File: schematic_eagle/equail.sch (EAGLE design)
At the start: 4 parts, among them U1 ATTINY85V-10P

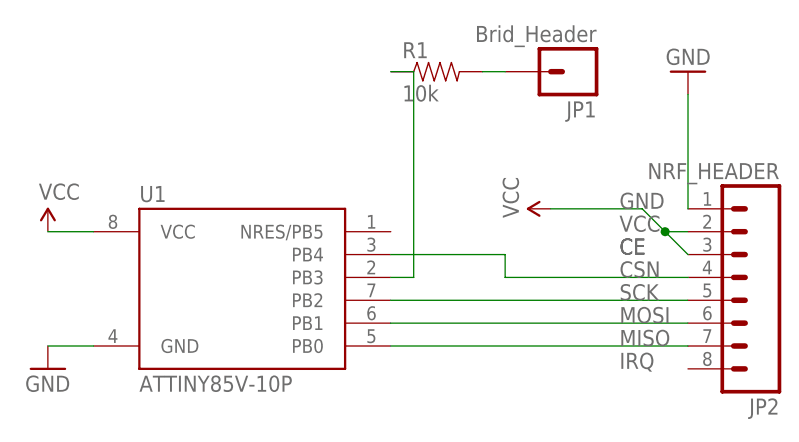
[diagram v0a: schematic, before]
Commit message: Updated schematic to include extra capacitor
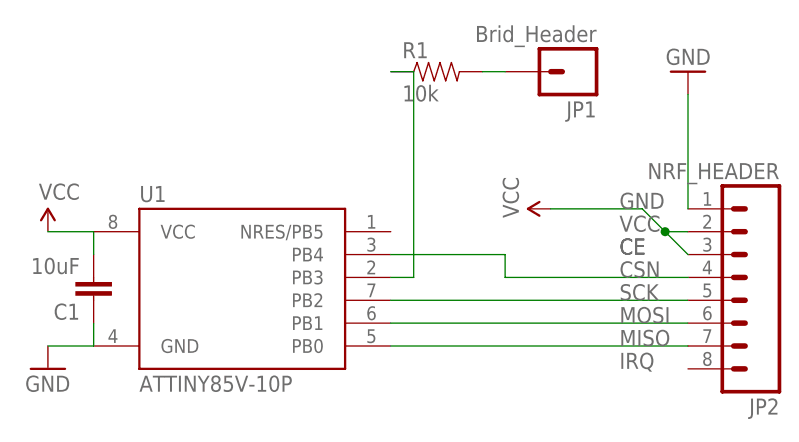
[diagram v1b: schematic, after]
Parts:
- added C1: 10uF, SparkFun-Capacitors:CAPEZ
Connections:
- net GND: now also C1.1
- net VCC: now also C1.2
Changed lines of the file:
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@@
 <grid distance="0.1" unitdist="inch" unit="inch" style="lines" multiple="1" display="no" altdistance="0.01" altunitdist="inch" altunit="inch"/>
 <layers>
-<layer number="1" name="Top" color="4" fill="1" visible="yes" active="no"/>
-<layer number="16" name="Bottom" color="1" fill="1" visible="yes" active="no"/>
-<layer number="17" name="Pads" color="2" fill="1" visible="yes" active="no"/>
-<layer number="18" name="Vias" color="2" fill="1" visible="yes" active="no"/>
-<layer number="19" name="Unrouted" color="6" fill="1" visible="yes" active="no"/>
-<layer number="20" name="Dimension" color="15" fill="1" visible="yes" active="no"/>
-<layer number="21" name="tPlace" color="7" fill="1" visible="yes" active="no"/>
-<layer number="22" name="bPlace" color="7" fill="1" visible="yes" active="no"/>
-<layer number="23" name="tOrigins" color="15" fill="1" visible="yes" active="no"/>
-<layer number="24" name="bOrigins" color="15" fill="1" visible="yes" active="no"/>
-<layer number="25" name="tNames" color="7" fill="1" visible="yes" active="no"/>
-<layer number="26" name="bNames" color="7" fill="1" visible="yes" active="no"/>
-<layer number="27" name="tValues" color="7" fill="1" visible="yes" active="no"/>
-<layer number="28" name="bValues" color="7" fill="1" visible="yes" active="no"/>
+<layer number="1" name="Top" color="4" fill="1" visible="no" active="no"/>
+<layer number="16" name="Bottom" color="1" fill="1" visible="no" active="no"/>
+<layer number="17" name="Pads" color="2" fill="1" visible="no" active="no"/>
+<layer number="18" name="Vias" color="2" fill="1" visible="no" active="no"/>
+<layer number="19" name="Unrouted" color="6" fill="1" visible="no" active="no"/>
+<layer number="20" name="Dimension" color="15" fill="1" visible="no" active="no"/>
+<layer number="21" name="tPlace" color="7" fill="1" visible="no" active="no"/>
+<layer number="22" name="bPlace" color="7" fill="1" visible="no" active="no"/>
+<layer number="23" name="tOrigins" color="15" fill="1" visible="no" active="no"/>
+<layer number="24" name="bOrigins" color="15" fill="1" visible="no" active="no"/>
+<layer number="25" name="tNames" color="7" fill="1" visible="no" active="no"/>
+<layer number="26" name="bNames" color="7" fill="1" visible="no" active="no"/>
+<layer number="27" name="tValues" color="7" fill="1" visible="no" active="no"/>
+<layer number="28" name="bValues" color="7" fill="1" visible="no" active="no"/>
 <layer number="29" name="tStop" color="7" fill="3" visible="no" active="no"/>
 <layer number="30" name="bStop" color="7" fill="6" visible="no" active="no"/>
@@
 <layer number="35" name="tGlue" color="7" fill="4" visible="no" active="no"/>
 <layer number="36" name="bGlue" color="7" fill="5" visible="no" active="no"/>
-<layer number="37" name="tTest" color="7" fill="1" visible="yes" active="no"/>
-<layer number="38" name="bTest" color="7" fill="1" visible="yes" active="no"/>
+<layer number="37" name="tTest" color="7" fill="1" visible="no" active="no"/>
+<layer number="38" name="bTest" color="7" fill="1" visible="no" active="no"/>
 <layer number="39" name="tKeepout" color="4" fill="11" visible="no" active="no"/>
 <layer number="40" name="bKeepout" color="1" fill="11" visible="no" active="no"/>
@@
 <layer number="44" name="Drills" color="7" fill="1" visible="no" active="no"/>
 <layer number="45" name="Holes" color="7" fill="1" visible="no" active="no"/>
-<layer number="46" name="Milling" color="3" fill="1" visible="yes" active="no"/>
-<layer number="47" name="Measures" color="7" fill="1" visible="yes" active="no"/>
-<layer number="48" name="Document" color="7" fill="1" visible="yes" active="no"/>
-<layer number="49" name="Reference" color="7" fill="1" visible="yes" active="no"/>
-<layer number="50" name="dxf" color="7" fill="1" visible="yes" active="no"/>
-<layer number="51" name="tDocu" color="7" fill="1" visible="yes" active="no"/>
-<layer number="52" name="bDocu" color="7" fill="1" visible="yes" active="no"/>
-<layer number="53" name="tGND_GNDA" color="7" fill="9" visible="yes" active="no"/>
-<layer number="54" name="bGND_GNDA" color="1" fill="9" visible="yes" active="no"/>
-<layer number="56" name="wert" color="7" fill="1" visible="yes" active="no"/>
-<layer number="57" name="tCAD" color="7" fill="1" visible="yes" active="no"/>
+<layer number="46" name="Milling" color="3" fill="1" visible="no" active="no"/>
+<layer number="47" name="Measures" color="7" fill="1" visible="no" active="no"/>
+<layer number="48" name="Document" color="7" fill="1" visible="no" active="no"/>
+<layer number="49" name="Reference" color="7" fill="1" visible="no" active="no"/>
+<layer number="50" name="dxf" color="7" fill="1" visible="no" active="no"/>
+<layer number="51" name="tDocu" color="7" fill="1" visible="no" active="no"/>
+<layer number="52" name="bDocu" color="7" fill="1" visible="no" active="no"/>
+<layer number="53" name="tGND_GNDA" color="7" fill="9" visible="no" active="no"/>
+<layer number="54" name="bGND_GNDA" color="1" fill="9" visible="no" active="no"/>
+<layer number="56" name="wert" color="7" fill="1" visible="no" active="no"/>
+<layer number="57" name="tCAD" color="7" fill="1" visible="no" active="no"/>
 <layer number="91" name="Nets" color="2" fill="1" visible="yes" active="yes"/>
 <layer number="92" name="Busses" color="1" fill="1" visible="yes" active="yes"/>
@@
 <part name="GND2" library="SparkFun-Aesthetics" deviceset="GND" device=""/>
 <part name="SUPPLY1" library="SparkFun-Aesthetics" deviceset="VCC" device=""/>
+<part name="C1" library="SparkFun-Capacitors" deviceset="CAP" device="EZ" value="10uF"/>
 </parts>
 <sheets>
@@
 <instance part="GND2" gate="1" x="116.84" y="124.46" rot="R180"/>
 <instance part="SUPPLY1" gate="G$1" x="101.6" y="109.22" rot="R90"/>
+<instance part="C1" gate="G$1" x="50.8" y="101.6" rot="R180"/>
 </instances>
 <busses>
@@
 <pinref part="SUPPLY2" gate="G$1" pin="VCC"/>
 <wire x1="50.8" y1="106.68" x2="45.72" y2="106.68" width="0.1524" layer="91"/>
+<pinref part="C1" gate="G$1" pin="2"/>
+<wire x1="50.8" y1="104.14" x2="50.8" y2="106.68" width="0.1524" layer="91"/>
 </segment>
 <segment>
@@
 <pinref part="GND1" gate="1" pin="GND"/>
 <wire x1="50.8" y1="93.98" x2="45.72" y2="93.98" width="0.1524" layer="91"/>
-</segment>
-<segment>
+<pinref part="C1" gate="G$1" pin="1"/>
+<wire x1="50.8" y1="96.52" x2="50.8" y2="93.98" width="0.1524" layer="91"/>
+</segment>
+<segment>
